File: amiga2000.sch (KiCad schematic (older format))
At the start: 0 parts

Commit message: urgh
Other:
- note removed: "done\n to review"
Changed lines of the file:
@@
 x done\n   to review
 Text Notes 5700 1300 0    50   ~ 0
-  done\n  to review
+x done\n   to review
 Text Notes 7250 1300 0    50   ~ 0
 x done\n   to review
@@
 x done\n   to review
 Text Notes 8750 2300 0    50   ~ 0
-  done\n  to review
+ x done\n   to review
 Text Notes 7300 2300 0    50   ~ 0
 x done\n   to review

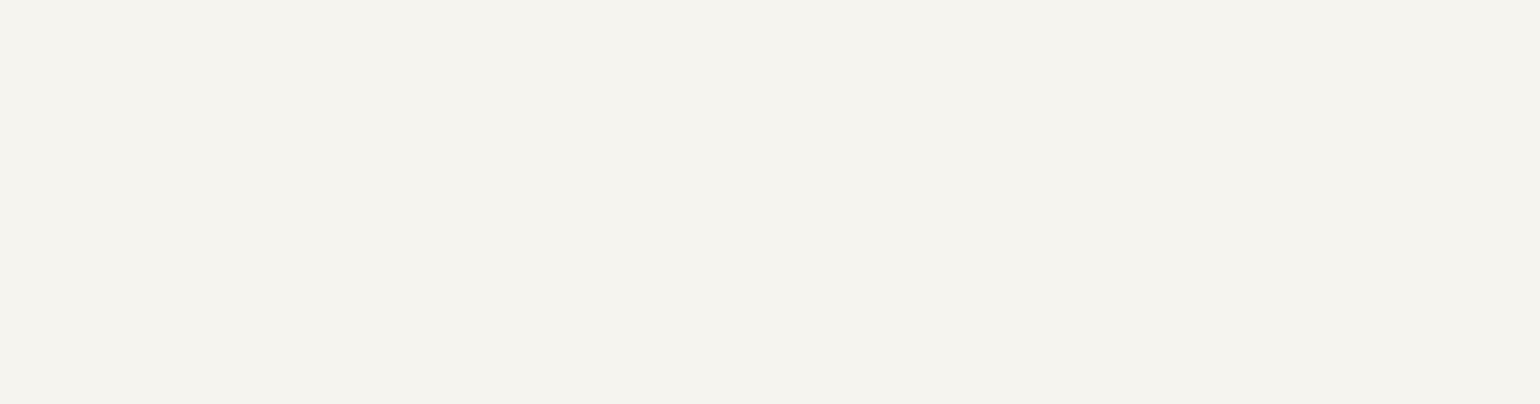
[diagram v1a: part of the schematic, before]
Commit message: Implemented various rev 6.2 fixes from forums and my own board
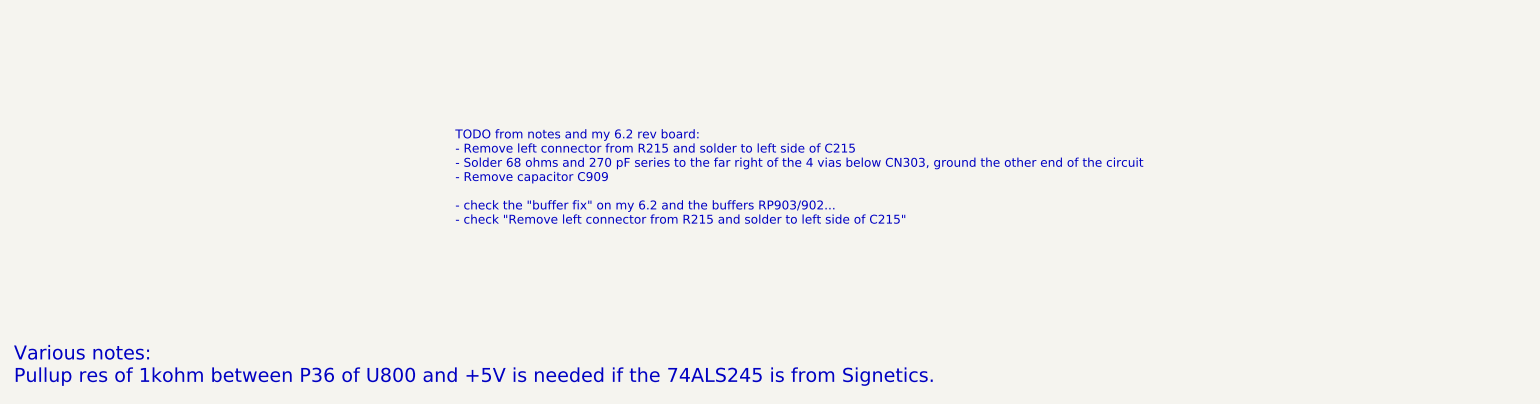
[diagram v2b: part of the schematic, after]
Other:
- note added: "TODO from notes and my 6.2 rev board:\n- Remove left connector from R215 and solder to left side of C215\n- Solder 68 ohms and 270 pF series to the far right of the 4 vias below CN303, ground the other end of the circuit\n- Remove capacitor C909\n\n- check the "buffer fix" on my 6.2 and the buffers RP903/902...\n- check "Remove left connector from R215 and solder to left side of C215""
- note added: "Various notes:\nPullup res of 1kohm between P36 of U800 and +5V is needed if the 74ALS245 is from Signetics."
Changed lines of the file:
@@
 Text Notes 1250 2300 0    50   ~ 0
 x done\n   to review
+Text Notes 1000 5100 0    79   ~ 0
+Various notes:\nPullup res of 1kohm between P36 of U800 and +5V is needed if the 74ALS245 is from Signetics.
+Text Notes 3500 4200 0    50   ~ 0
+TODO from notes and my 6.2 rev board:\n- Remove left connector from R215 and solder to left side of C215\n- Solder 68 ohms and 270 pF series to the far right of the 4 vias below CN303, ground the other end of the circuit\n- Remove capacitor C909\n\n- check the "buffer fix" on my 6.2 and the buffers RP903/902...\n- check "Remove left connector from R215 and solder to left side of C215"
 $EndSCHEMATC

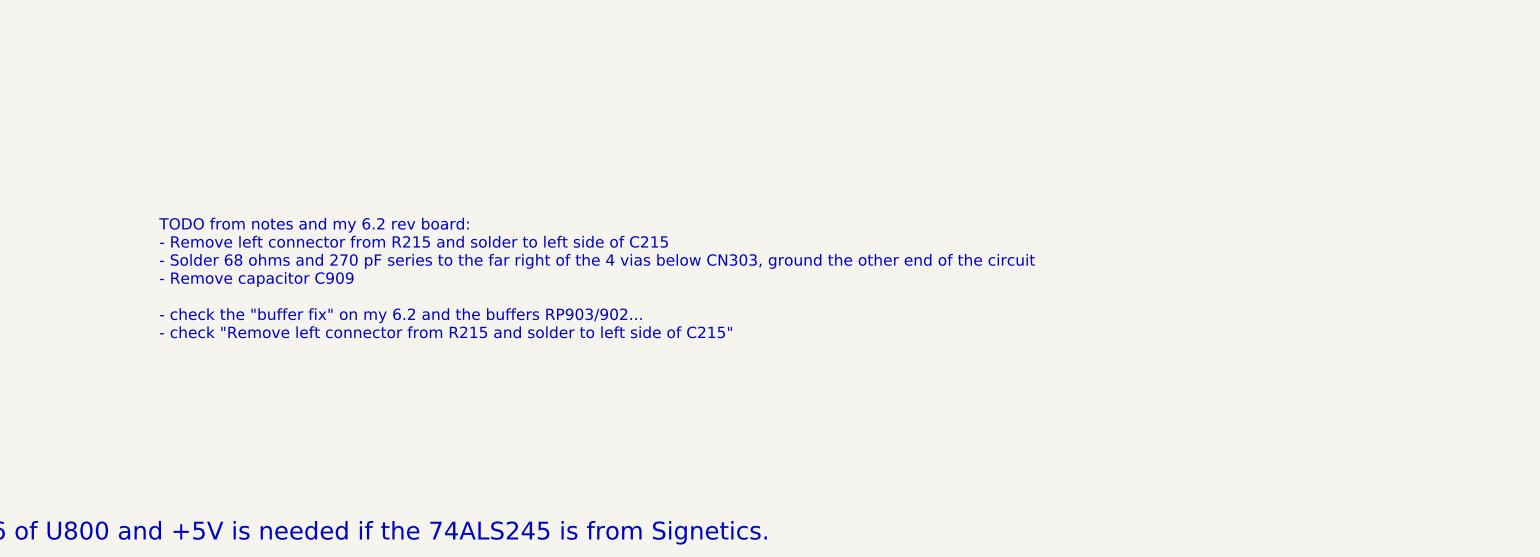
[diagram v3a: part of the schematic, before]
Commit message: Rev 6.2 fixes are now documented properly
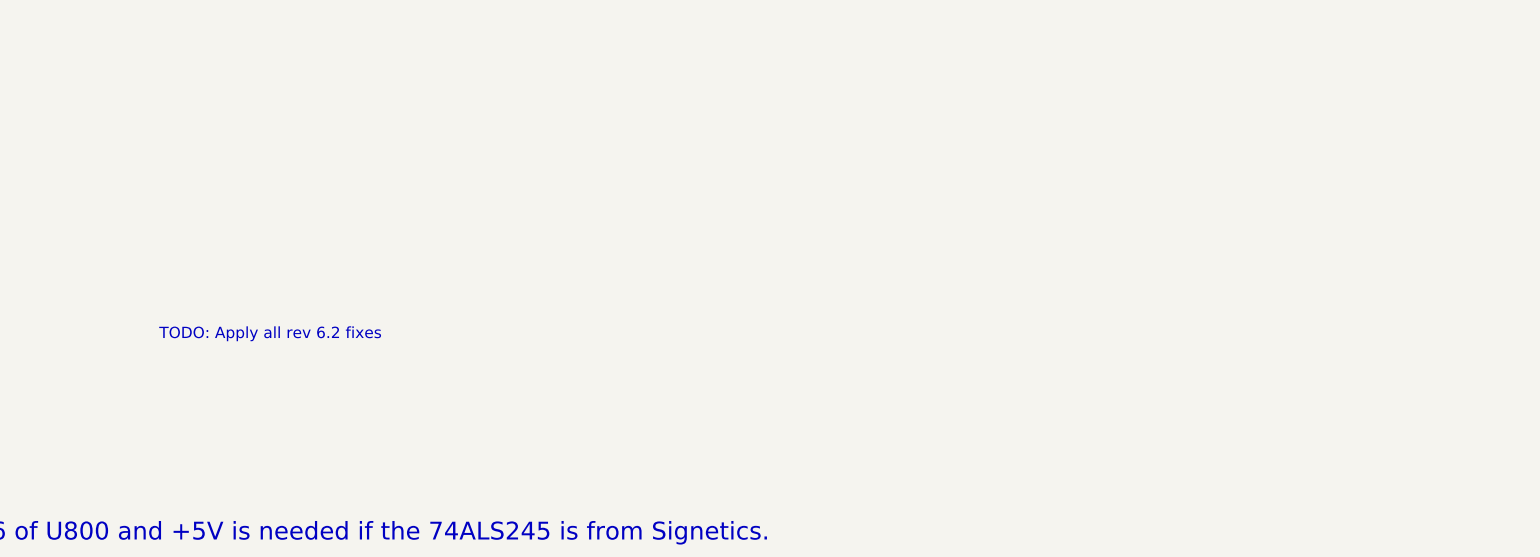
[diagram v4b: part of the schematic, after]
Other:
- note added: "TODO: Apply all rev 6.2 fixes"
- note removed: "TODO from notes and my 6.2 rev board:\n- Remove left connector from R215 and solder to left side of C215\n- Solder 68 ohms and 270 pF series to the far right of the 4 vias below CN303, ground the other end of the circuit\n- Remove capacitor C909\n\n- check the "buffer fix" on my 6.2 and the buffers RP903/902...\n- check "Remove left connector from R215 and solder to left side of C215""
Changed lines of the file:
@@
 Various notes:\nPullup res of 1kohm between P36 of U800 and +5V is needed if the 74ALS245 is from Signetics.
 Text Notes 3500 4200 0    50   ~ 0
-TODO from notes and my 6.2 rev board:\n- Remove left connector from R215 and solder to left side of C215\n- Solder 68 ohms and 270 pF series to the far right of the 4 vias below CN303, ground the other end of the circuit\n- Remove capacitor C909\n\n- check the "buffer fix" on my 6.2 and the buffers RP903/902...\n- check "Remove left connector from R215 and solder to left side of C215"
+TODO: Apply all rev 6.2 fixes
 $EndSCHEMATC

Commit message: REV 6.2 fixes applied
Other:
- note removed: "TODO: Apply all rev 6.2 fixes"
- note removed: "Various notes:\nPullup res of 1kohm between P36 of U800 and +5V is needed if the 74ALS245 is from Signetics."
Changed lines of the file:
@@
 Text Notes 1250 2300 0    50   ~ 0
 x done\n   to review
-Text Notes 1000 5100 0    79   ~ 0
-Various notes:\nPullup res of 1kohm between P36 of U800 and +5V is needed if the 74ALS245 is from Signetics.
-Text Notes 3500 4200 0    50   ~ 0
-TODO: Apply all rev 6.2 fixes
 $EndSCHEMATC

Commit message: Document rev 6.3 and 6.4 fixes here
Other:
- note added: "Rev 6.3 fixes :\n - Kickstart 2.03 and Denise 8373\n\nRev 6.4 fixes :\n - Agnus 8375\n - Instead of R101, add a capacitor (100nF) from right side of R101 to ground"
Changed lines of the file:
@@
 Text Notes 1250 2300 0    50   ~ 0
 x done\n   to review
+Text Notes 950  5550 0    157  ~ 0
+Rev 6.3 fixes :\n - Kickstart 2.03 and Denise 8373\n\nRev 6.4 fixes :\n - Agnus 8375\n - Instead of R101, add a capacitor (100nF) from right side of R101 to ground
 $EndSCHEMATC

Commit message: hmmmm
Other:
- note added: "review 1 :\nreview 2 :"
- note removed: "x done\n to review"
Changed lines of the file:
@@
 F1 "coprocessor slot.sch" 50
 $EndSheet
-Text Notes 1200 1300 0    50   ~ 0
-x done\n   to review
-Text Notes 2750 1300 0    50   ~ 0
-x done\n   to review
-Text Notes 4250 1300 0    50   ~ 0
-x done\n   to review
-Text Notes 5700 1300 0    50   ~ 0
-x done\n   to review
-Text Notes 7250 1300 0    50   ~ 0
-x done\n   to review
-Text Notes 8750 1300 0    50   ~ 0
-x done\n   to review
-Text Notes 8750 2300 0    50   ~ 0
- x done\n   to review
-Text Notes 7300 2300 0    50   ~ 0
-x done\n   to review
-Text Notes 5750 2300 0    50   ~ 0
-x done\n   to review
-Text Notes 4300 2300 0    50   ~ 0
-x done\n   to review
-Text Notes 2750 2300 0    50   ~ 0
-x done\n   to review
-Text Notes 1250 2300 0    50   ~ 0
-x done\n   to review
-Text Notes 950  5550 0    157  ~ 0
+Text Notes 1050 1350 0    79   ~ 0
+review 1 :\nreview 2 :
+Text Notes 900  6350 0    157  ~ 0
 Rev 6.3 fixes :\n - Kickstart 2.03 and Denise 8373\n\nRev 6.4 fixes :\n - Agnus 8375\n - Instead of R101, add a capacitor (100nF) from right side of R101 to ground
+Text Notes 1050 2350 0    79   ~ 0
+review 1 :\nreview 2 :
+Text Notes 2550 2350 0    79   ~ 0
+review 1 :\nreview 2 :
+Text Notes 4050 2350 0    79   ~ 0
+review 1 :\nreview 2 :
+Text Notes 5550 2350 0    79   ~ 0
+review 1 :\nreview 2 :
+Text Notes 5550 1350 0    79   ~ 0
+review 1 :\nreview 2 :
+Text Notes 4050 1350 0    79   ~ 0
+review 1 :\nreview 2 :
+Text Notes 2550 1350 0    79   ~ 0
+review 1 :\nreview 2 :
+Text Notes 7050 1350 0    79   ~ 0
+review 1 :\nreview 2 :
+Text Notes 8550 1350 0    79   ~ 0
+review 1 :\nreview 2 :
+Text Notes 8550 2350 0    79   ~ 0
+review 1 :\nreview 2 :
+Text Notes 7050 2350 0    79   ~ 0
+review 1 :\nreview 2 :
 $EndSCHEMATC

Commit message: Review started; oopsie whoopsie
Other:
- note added: "review 1 : ok\nreview 2 :"
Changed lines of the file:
@@
 $EndSheet
 Text Notes 1050 1350 0    79   ~ 0
-review 1 :\nreview 2 :
+review 1 : ok\nreview 2 :
 Text Notes 900  6350 0    157  ~ 0
 Rev 6.3 fixes :\n - Kickstart 2.03 and Denise 8373\n\nRev 6.4 fixes :\n - Agnus 8375\n - Instead of R101, add a capacitor (100nF) from right side of R101 to ground
